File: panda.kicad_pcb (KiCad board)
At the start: 2 copper layers, 100 x 125 mm, 116 parts, among them J1 PIN6-9_Breakout, J10 Screw_Terminal_01x02, J11 24V_Lockout_Key_Switch, J12 XT60-M, J13 PT_1, J14 PT_4, J15 PT_2, J16 PT_5, J17 PT_3, J18 PT_6, J19 4-Pin Load Cell, J2 PIN10-13_Breakout, J20 5-Pin Load Cell, J21 Ignitor Screw Terminal, J3 Valve_1_PWR, J4 Valve_4_PWR, J5 Valve_2_PWR, J6 Valve_5_PWR, J7 Valve_3_PWR, J8 Valve_6_PWR, J9 Screw_Terminal_01x04, K1 G5LE-1, K2 G5LE-1, Q1 BSS138, Q2 BSS138, Q3 BSS138, Q4 BSS138, Q5 BSS138, Q6 BSS138, Q7 BSS138, Q8 BSS138, U1 ESP32-S3, U2 ADS112C04, U3 ADS112C04, U4 ADS112C04, U5 ADS112C04, U6 XC6206P332MR, U7 TPS5430DDA, U8 TPS5430DDA

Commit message: Switch relay driving FETs to low side. Relays changed to SPST instead of SPDT
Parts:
- K1, K2: value G5LE-1 -> G5Q-1A DC24; footprint Relay_THT:Relay_SPDT_Omron-G5LE-1 -> Relay_THT:Relay_SPST_Omron-G5Q-1A
- R31, R32, R33, R34, R35, R36: value 250 -> 250R
- moved R38 9.77 mm to (149.0, 56.2)
- moved R37 9.76 mm to (149.0, 55.0), turned to 180 degrees
- moved D10 9.24 mm to (154.8, 52.8)
- moved Q8 7.12 mm to (148.4, 52.4)
- moved R25 4.72 mm to (135.6, 56.0), turned to 180 degrees
- moved R26 4.68 mm to (135.6, 57.2)
- moved D7 4.53 mm to (141.4, 52.8)
- moved K1 3.81 mm to (144.8, 48.5), turned to 90 degrees
- moved K2 2.41 mm to (157.8, 48.5), turned to 90 degrees
- moved Q7 2.11 mm to (135.0, 53.4)
- renumbered SDA to TP1, SCL to TP2
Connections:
- D10 pad 1: /Ignitor Control/IGNITOR_RLY_+VE -> +24V_SAFE
- D10 pad 2: GND -> Net-(D10-A)
- D7 pad 1: /Power Regulation/LOCKOUT_RLY_+VE -> +24V
- D7 pad 2: GND -> Net-(D7-A)
- K1 pad 1: /Power Regulation/+24V_POST_LOCKOUT -> +24V
- K1 pad 2: /Power Regulation/LOCKOUT_RLY_+VE -> /Power Regulation/+24V_POST_LOCKOUT
- K1 pad 5: GND -> Net-(D7-A)
- K2 pad 2: /Ignitor Control/IGNITOR_RLY_+VE -> +24V_SAFE
- K2 pad 5: GND -> Net-(D10-A)
- Q7 pad 2: +24V -> GND
- Q7 pad 3: /Power Regulation/LOCKOUT_RLY_+VE -> Net-(D7-A)
- Q8 pad 2: +24V_SAFE -> GND
- Q8 pad 3: /Ignitor Control/IGNITOR_RLY_+VE -> Net-(D10-A)
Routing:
- net /Power Regulation/LOCKOUT_RLY_+VE: track 19.8 -> 0.00 mm
- net /Ignitor Control/IGNITOR_RLY_+VE: track 19.8 -> 0.00 mm
- net +24V: track 420.2 -> 432.9 mm
- net Net-(D10-A): track 0.00 -> 11.1 mm
- net /Ignitor Control/IGNITOR_SOURCE: track 48.7 -> 37.7 mm
- net Net-(D7-A): track 0.00 -> 10.4 mm
- net IGNITOR_CTL: track 16.9 -> 22.8 mm
- net SAFE_24V_CTL: track 25.4 -> 29.8 mm
- net +24V_SAFE: track 100.3 -> 102.8 mm
- net GND: track 46.3 -> 44.7 mm, vias 24 -> 21
- net /Power Regulation/LOCKOUT_RLY_CTRL_FET: track 3.68 -> 2.78 mm

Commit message: Actually fix XT60 silkscreen and placement
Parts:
- removed the G*** at (158.9, 66.1)
- moved K1 3.14 mm to (141.7, 48.1)
- moved K2 3.14 mm to (154.7, 48.1)
- moved R37 3.14 mm to (145.9, 54.6)
- moved R38 3.14 mm to (145.9, 55.8)
- moved Q7 3.14 mm to (131.9, 53.0)
- moved Q8 3.14 mm to (145.3, 52.0)
- moved R25 3.14 mm to (132.5, 55.6)
- moved R26 3.14 mm to (132.5, 56.8)
- moved D10 3.14 mm to (151.7, 52.4)
- moved D7 3.14 mm to (138.3, 52.4)
- moved J12 2.56 mm to (126.2, 45.9)
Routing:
- net +24V: track 432.9 -> 428.1 mm
- net /Power Regulation/+24V_POST_LOCKOUT: track 33.5 -> 30.3 mm
- net /Ignitor Control/IGNITOR_SOURCE: track 37.7 -> 34.4 mm
- net SAFE_24V_CTL: track 29.8 -> 33.1 mm
- net +24V_SAFE: track 102.8 -> 100.0 mm
- net IGNITOR_CTL: track 22.8 -> 24.4 mm

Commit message: Swap PT3 and PT4 connectors so they are connected to teh proper pins
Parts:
- moved J14 9.14 mm to (187.4, 138.8)
- moved J17 8.96 mm to (178.3, 138.8)
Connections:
- J14 pad 2: PT_READING_4 -> PT_READING_3
- J17 pad 2: PT_READING_3 -> PT_READING_4
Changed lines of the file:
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@@
 	(footprint "Connector_JST:JST_XH_B2B-XH-A_1x02_P2.50mm_Vertical"
 		(layer "F.Cu")
-		(at 187.262501 138.75)
+		(at 178.3 138.75)
 		(descr "JST XH series connector, B2B-XH-A (http://www.jst-mfg.com/product/pdf/eng/eXH.pdf), generated with kicad-footprint-generator")
 		(tags "connector JST XH vertical")
@@
 			(layers "*.Cu" "*.Mask")
 			(remove_unused_layers no)
-			(net 26 "PT_READING_3")
+			(net 27 "PT_READING_4")
 			(pinfunction "Pin_2")
 			(pintype "passive")
@@
 	(footprint "Connector_JST:JST_XH_B2B-XH-A_1x02_P2.50mm_Vertical"
 		(layer "F.Cu")
-		(at 178.262501 138.75)
+		(at 187.4 138.8)
 		(descr "JST XH series connector, B2B-XH-A (http://www.jst-mfg.com/product/pdf/eng/eXH.pdf), generated with kicad-footprint-generator")
 		(tags "connector JST XH vertical")
@@
 			(layers "*.Cu" "*.Mask")
 			(remove_unused_layers no)
-			(net 27 "PT_READING_4")
+			(net 26 "PT_READING_3")
 			(pinfunction "Pin_2")
 			(pintype "passive")
@@
 				"c2d707f4-c589-45be-a4e5-f1216058ba92" "c53e86fc-e412-4a99-8569-db2e16a4568e"
 				"c96ee9c1-957b-47e7-a496-9d07a8ef65c1" "d07868b0-93fb-46ed-8fe2-f1341275527b"
-				"d07868b0-93fb-46ed-8fe2-f1341275527b" "d3ef4f30-dd92-492b-9b90-6c96d7b27b1c"
-				"dce0ce9b-604a-4b68-bb71-2f51e01cb351" "eb4fe7c9-751b-4024-8bff-6fe5d6652741"
-				"f31896e9-2716-4ede-b07b-ca2df04834f9"
+				"d3ef4f30-dd92-492b-9b90-6c96d7b27b1c" "dce0ce9b-604a-4b68-bb71-2f51e01cb351"
+				"eb4fe7c9-751b-4024-8bff-6fe5d6652741" "f31896e9-2716-4ede-b07b-ca2df04834f9"
 			)
 		)
@@
 				"4676d2f9-a1e1-4cbb-ba3e-26eb225c8346" "48c95736-b839-4eba-bf88-c32424fc2f4a"
 				"4a632986-8b94-4b68-a8b9-1b316e8da8c6" "4dbea90c-996e-49c7-8cc7-35cba6247e63"
-				"537a95c3-721c-4c6b-a6ac-392c8ff340d2" "537a95c3-721c-4c6b-a6ac-392c8ff340d2"
-				"54676ae9-67dd-43c3-9dac-1a1aa898e2f8" "5708a558-de7f-4510-a968-dc604294bcfe"
-				"61d3b5dc-eeac-4d8e-a833-3230edbd5ce4" "72684f53-c3fa-4d1f-8d8c-17e517f05a17"
-				"7b2bc166-f06b-4eb1-8d0b-953cbb8b7959" "7d5a21d3-475d-42ad-a46b-23a2f6595e38"
-				"7f6478ec-5b00-417a-9ffb-c4c02532cf02" "83147ee5-7a61-4b9e-bd70-37245b788deb"
+				"537a95c3-721c-4c6b-a6ac-392c8ff340d2" "54676ae9-67dd-43c3-9dac-1a1aa898e2f8"
+				"5708a558-de7f-4510-a968-dc604294bcfe" "61d3b5dc-eeac-4d8e-a833-3230edbd5ce4"
+				"72684f53-c3fa-4d1f-8d8c-17e517f05a17" "7b2bc166-f06b-4eb1-8d0b-953cbb8b7959"
+				"7d5a21d3-475d-42ad-a46b-23a2f6595e38" "7f6478ec-5b00-417a-9ffb-c4c02532cf02"
 				"83147ee5-7a61-4b9e-bd70-37245b788deb" "88d6741e-8d35-48a3-b48e-2b5854aa8dc0"
 				"9008c045-1770-48db-bc1f-44d886bb9e68" "90ae0285-da63-4916-826c-2d5b471975b7"
 				"9918f291-fadf-4ff6-9fc6-9444dbd68b86" "a2dc5d06-c3b7-4c02-9762-4462126ae29e"
-				"a7a7b65d-c7d1-496e-9211-2dccfbec3615" "a7a7b65d-c7d1-496e-9211-2dccfbec3615"
-				"ace83577-5fe0-46c6-9cad-13fba02db98b" "c1c6e622-00e1-420a-8a5d-f9f55b86e6ba"
-				"c60040a4-4fc9-4539-be0c-7cd3ae8ab98f" "c60040a4-4fc9-4539-be0c-7cd3ae8ab98f"
+				"a7a7b65d-c7d1-496e-9211-2dccfbec3615" "ace83577-5fe0-46c6-9cad-13fba02db98b"
+				"c1c6e622-00e1-420a-8a5d-f9f55b86e6ba" "c60040a4-4fc9-4539-be0c-7cd3ae8ab98f"
 				"cc37c910-ac21-4590-9744-fc68181f1ec2" "ccafc2b7-fcbe-44e1-9648-d182a990cfee"
 				"cf9046d8-7816-48bd-9071-a4f6fe10ec60" "d5a76beb-f7b5-43da-ad01-9a860a26e286"

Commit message: Actually fix PT3 and PT4 mapping
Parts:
- moved R32 9.06 mm to (189.0, 143.8)
- moved R35 8.85 mm to (180.1, 143.8)
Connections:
- J14 pad 2: PT_READING_3 -> PT_READING_4
- J17 pad 2: PT_READING_4 -> PT_READING_3
- U5 pad 6: PT_READING_4 -> PT_READING_3
- U5 pad 7: PT_READING_3 -> PT_READING_4
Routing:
- net PT_READING_3: track 26.2 -> 28.2 mm
- net PT_READING_4: track 28.1 -> 26.4 mm
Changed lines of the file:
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@@
 			(layers "*.Cu" "*.Mask")
 			(remove_unused_layers no)
-			(net 27 "PT_READING_4")
+			(net 26 "PT_READING_3")
 			(pinfunction "Pin_2")
 			(pintype "passive")
@@
 		)
 		(property "Value" "PT_4"
-			(at 1.25 4.6 0)
+			(at -7.6 4.6 0)
 			(layer "F.Fab")
 			(effects
@@
 			(layers "*.Cu" "*.Mask")
 			(remove_unused_layers no)
-			(net 26 "PT_READING_3")
+			(net 27 "PT_READING_4")
 			(pinfunction "Pin_2")
 			(pintype "passive")
@@
 	(footprint "Resistor_SMD:R_0603_1608Metric"
 		(layer "F.Cu")
-		(at 179.937501 143.75 180)
+		(at 189 143.8 180)
 		(descr "Resistor SMD 0603 (1608 Metric), square (rectangular) end terminal, IPC_7351 nominal, (Body size source: IPC-SM-782 page 72, https://www.pcb-3d.com/wordpress/wp-content/uploads/ipc-sm-782a_amendment_1_and_2.pdf), generated with kicad-footprint-generator")
 		(tags "resistor")
@@
 	(footprint "Resistor_SMD:R_0603_1608Metric"
 		(layer "F.Cu")
-		(at 188.937501 143.75 180)
+		(at 180.087501 143.75 180)
 		(descr "Resistor SMD 0603 (1608 Metric), square (rectangular) end terminal, IPC_7351 nominal, (Body size source: IPC-SM-782 page 72, https://www.pcb-3d.com/wordpress/wp-content/uploads/ipc-sm-782a_amendment_1_and_2.pdf), generated with kicad-footprint-generator")
 		(tags "resistor")
@@
 			(layers "F.Cu" "F.Mask" "F.Paste")
 			(roundrect_rratio 0.25)
-			(net 27 "PT_READING_4")
+			(net 26 "PT_READING_3")
 			(pinfunction "AIN3")
 			(pintype "input")
@@
 			(layers "F.Cu" "F.Mask" "F.Paste")
 			(roundrect_rratio 0.25)
-			(net 26 "PT_READING_3")
+			(net 27 "PT_READING_4")
 			(pinfunction "AIN2")
 			(pintype "input")
@@
 	)
 	(segment
-		(start 188.262501 119.950002)
-		(end 187.512499 119.2)
+		(start 180.912501 143.75)
+		(end 181.163501 143.499)
 		(width 0.2)
 		(layer "F.Cu")
@@
 	)
 	(segment
-		(start 187.512499 119.2)
-		(end 186.775 119.2)
+		(start 180.8 138.75)
+		(end 180.8 130.2)
+		(width 0.2)
+		(layer "F.Cu")
+		(net 26)
+	)
+	(segment
+		(start 184.6 126.4)
+		(end 184.6 119.987501)
 		(width 0.2)
 		(layer "F.Cu")
@@
 	)
 	(segment
-		(start 188.262501 126.25)
-		(end 188.262501 119.950002)
+		(start 180.8 130.2)
+		(end 184.6 126.4)
 		(width 0.2)
 		(layer "F.Cu")
@@
 	)
 	(segment
-		(start 189.762501 138.75)
-		(end 189.762501 143.75)
+		(start 184.6 119.987501)
+		(end 186.037501 118.55)
 		(width 0.2)
 		(layer "F.Cu")
@@
 	)
 	(segment
-		(start 189.762501 138.75)
-		(end 189.762501 127.75)
+		(start 181.163501 143.499)
+		(end 181.163501 138.75)
 		(width 0.2)
 		(layer "F.Cu")
@@
 	)
 	(segment
-		(start 189.762501 127.75)
-		(end 188.262501 126.25)
+		(start 186.037501 118.55)
+		(end 186.775 118.55)
 		(width 0.2)
 		(layer "F.Cu")
@@
 	)
 	(segment
-		(start 180.762501 130.25)
-		(end 184.762501 126.25)
+		(start 189.9 127.9)
+		(end 188.2 126.2)
 		(width 0.2)
 		(layer "F.Cu")
@@
 	)
 	(segment
-		(start 180.762501 138.75)
-		(end 180.762501 130.25)
+		(start 188.2 126.2)
+		(end 188.2 119.6)
 		(width 0.2)
 		(layer "F.Cu")
@@
 	)
 	(segment
-		(start 184.762501 119.825)
-		(end 186.037501 118.55)
+		(start 189.825 143.8)
+		(end 189.825 138.875)
 		(width 0.2)
 		(layer "F.Cu")
@@
 	)
 	(segment
-		(start 186.037501 118.55)
-		(end 186.775 118.55)
+		(start 188.2 119.6)
+		(end 187.8 119.2)
 		(width 0.2)
 		(layer "F.Cu")
@@
 	)
 	(segment
-		(start 184.762501 126.25)
-		(end 184.762501 119.825)
+		(start 187.8 119.2)
+		(end 186.775 119.2)
 		(width 0.2)
 		(layer "F.Cu")
@@
 	)
 	(segment
-		(start 180.762501 138.75)
-		(end 180.762501 143.75)
+		(start 189.9 138.8)
+		(end 189.9 127.9)
 		(width 0.2)
 		(layer "F.Cu")

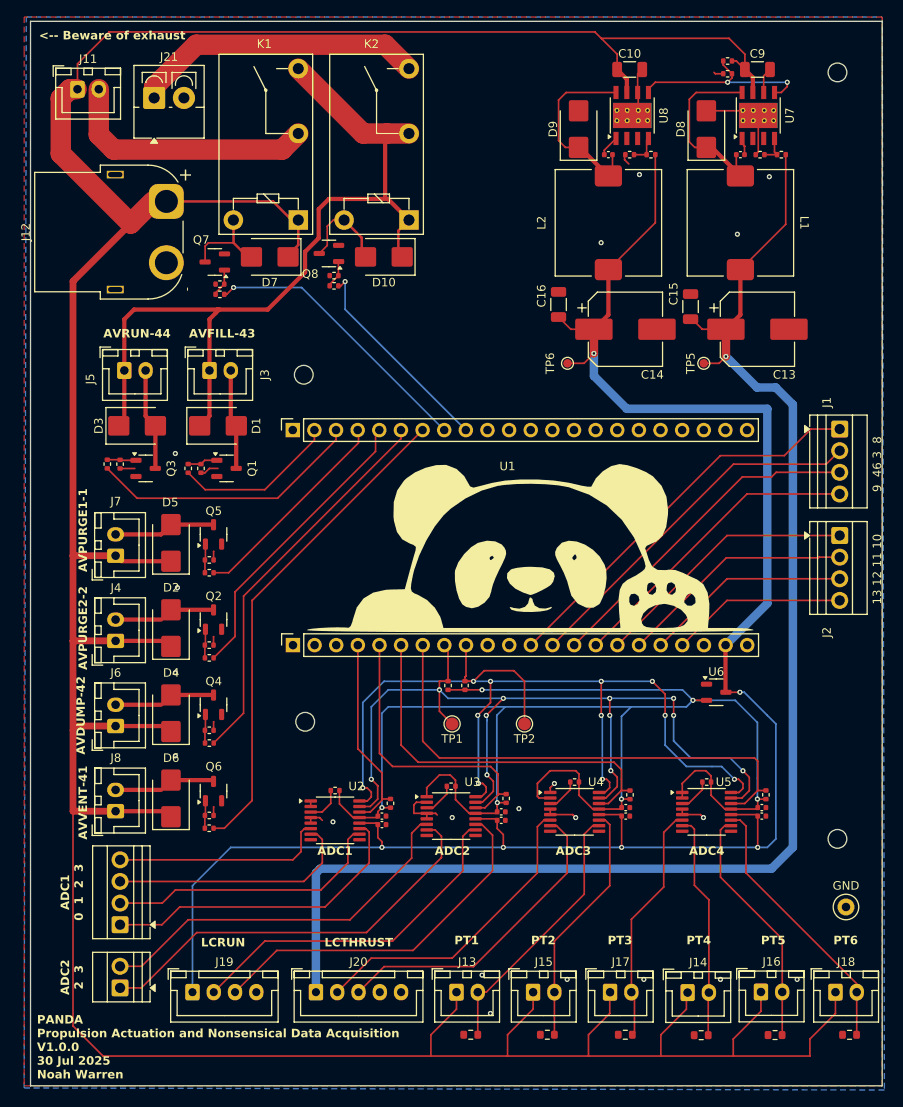
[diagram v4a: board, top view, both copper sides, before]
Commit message: Update thrust LC to take +5V. Remove +10V rail
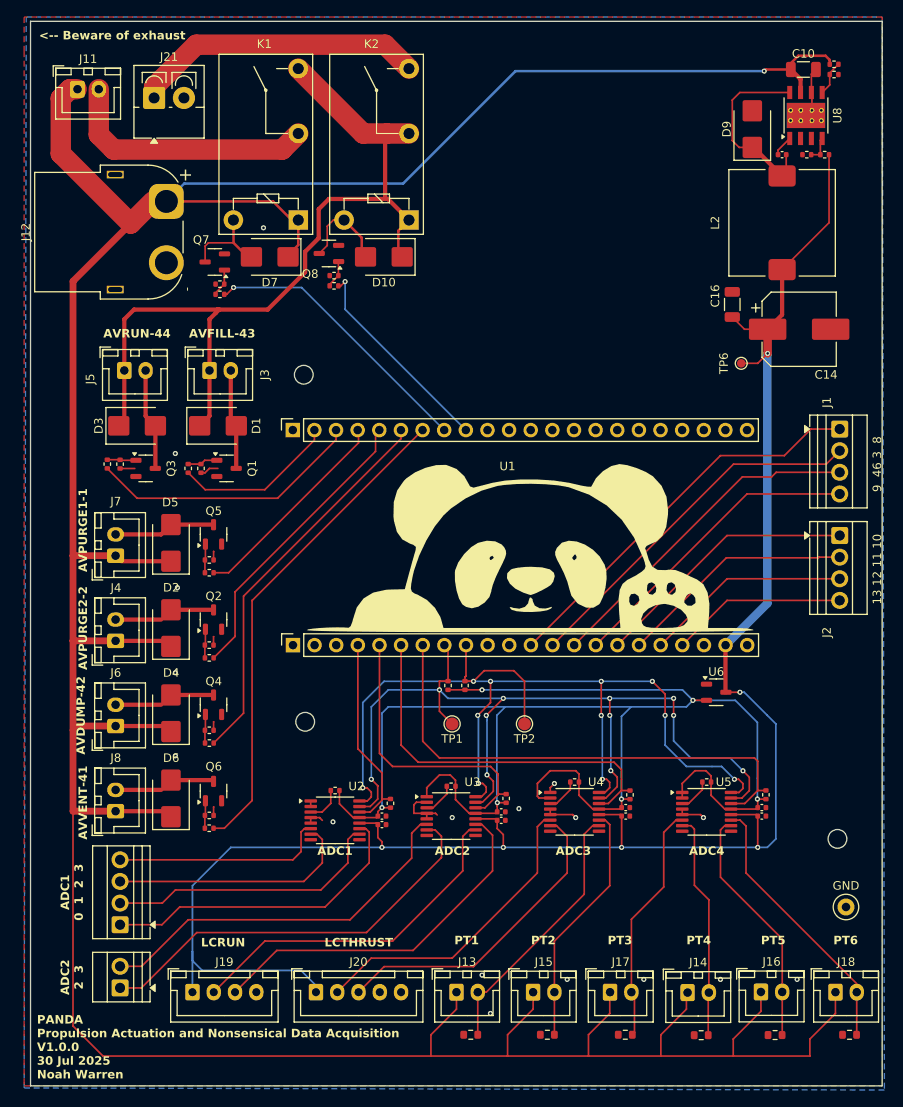
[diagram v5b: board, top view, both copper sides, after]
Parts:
- removed C11: 10nF, Capacitor_SMD:C_0402_1005Metric
- removed C13: 220uF, Capacitor_SMD:CP_Elec_8x10.5
- removed C15, C9: 10uF, Capacitor_SMD:C_1206_3216Metric
- removed D8: SK44BL, Diode_SMD:D_SMB
- removed L1: 22uH 4A, Inductor_SMD:L_12.5x12.5mm_SXNSMDRS1275
- removed R27: 10k, Resistor_SMD:R_0402_1005Metric
- removed R28: 1.4K, Resistor_SMD:R_0402_1005Metric
- removed the REF** at (205.0, 30.8)
- removed TP5: TP_+10V, TestPoint:TestPoint_Pad_D1.0mm
- removed U7: TPS5430DDA, Package_SO:TI_SO-PowerPAD-8_ThermalVias
- moved R30 20.8 mm to (201.4, 40.4)
- moved C10 20.4 mm to (201.0, 30.4)
- moved C12 20.4 mm to (198.5, 40.4)
- moved C14 20.4 mm to (200.5, 60.9)
- moved C16 20.4 mm to (192.6, 58.0)
- moved D9 20.4 mm to (195.0, 37.4)
- moved L2 20.4 mm to (198.5, 48.4)
- moved R29 20.4 mm to (203.5, 40.4)
- moved U8 20.4 mm to (201.3, 35.8)
- moved TP6 20.4 mm to (193.7, 64.9)
- moved R23 12.5 mm to (204.6, 29.8), turned to 0 degrees
- moved R24 12.5 mm to (204.6, 31.0), turned to 0 degrees
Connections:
- J20 pad 1: +10V -> +5V
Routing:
- net +10V: track 167.9 -> 0.00 mm, vias 1 -> 0
- net /Power Regulation/+10V_REG_PH: track 21.9 -> 0.00 mm
- net /Power Regulation/VREG_EN: track 22.4 -> 4.10 mm, vias 2 -> 0
- net GND: track 44.7 -> 30.2 mm, vias 21 -> 18
- net +24V: track 428.1 -> 418.9 mm, vias 0 -> 1
- net /Power Regulation/+10V_SENSE: track 3.79 -> 0.00 mm
- net /Power Regulation/+10V_REG_BOOT: track 2.03 -> 0.00 mm
- net +5V: track 223.0 -> 222.5 mm
